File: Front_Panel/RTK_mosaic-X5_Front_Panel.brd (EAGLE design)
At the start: 158.6 x 41 mm, 29 parts

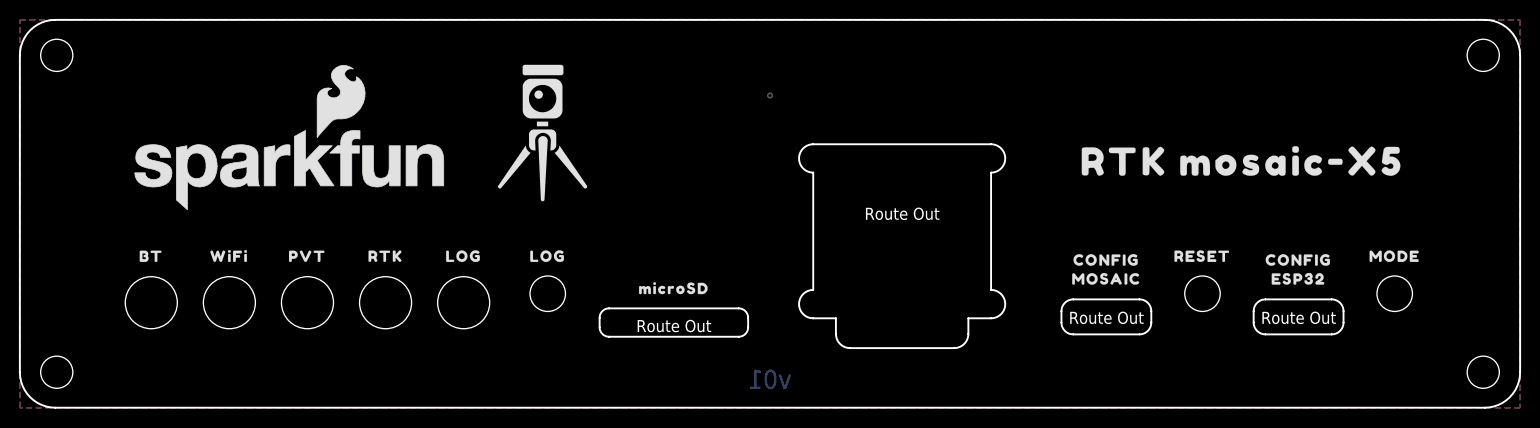
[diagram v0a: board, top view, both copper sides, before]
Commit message: Update front panel with new 1.3" OLED
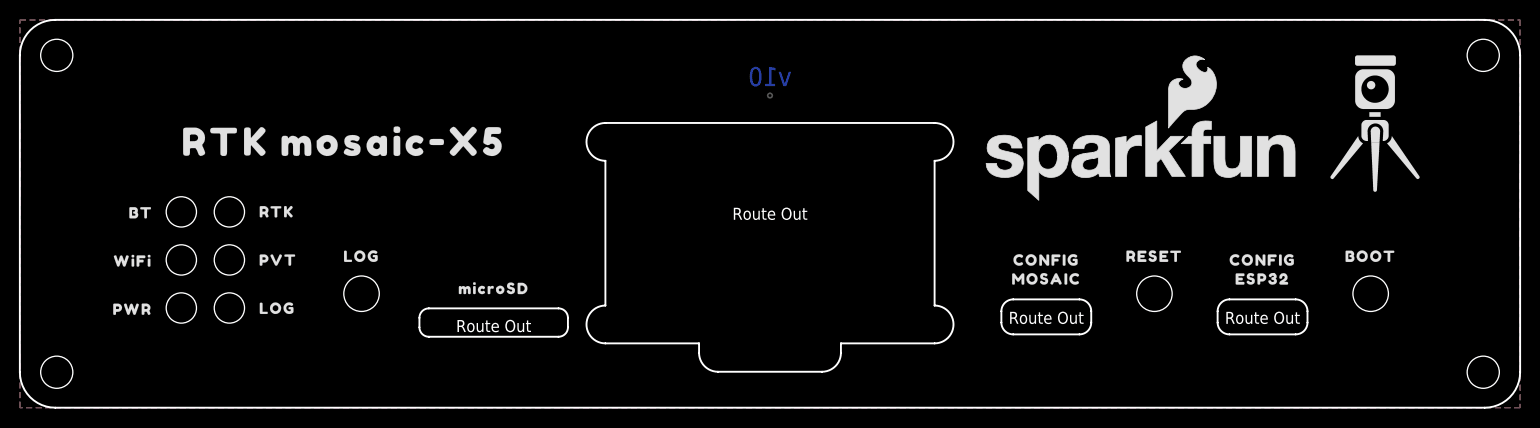
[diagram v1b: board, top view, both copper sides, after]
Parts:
- removed LED, LED5, LED6, LED7, LED8: LED_DIO-13847, SparkFun-Enclosure-Panel:LED
- removed U$2: (no value), output:MODE0
- added U$16, U$5: CBI_LED_TRIPLE-3MM_DIO-19990, SparkFun-Enclosure-Panel:CBI_LED_TRIPLE-3MM
- added U$17: (no value), output:PWR0
- added U$18: (no value), output:BOOT0
- OLED: value OLED_14532 -> OLED_1.3_128X64; device SparkFun-Enclosure-Panel:OLED -> SparkFun-Enclosure-Panel:OLED-1.3-128X64
- moved U$15 95.0 mm to (-45.0, 20.1)
- moved LOGO1 90.0 mm to (39.1, 18.1)
- moved U$6 20.5 mm to (-52.1, 2.50)
- moved RESET1 19.7 mm to (-43.2, 0.00)
- moved U$4 19.7 mm to (-43.2, 8.00)
- moved MICRO_SD 19.1 mm to (-29.2, 0.00)
- moved U$7 19.1 mm to (-29.2, 4.60)
- moved OLED 14.0 mm to (0.00, 12.5)
- moved U$14 12.4 mm to (-52.1, 12.7)
- moved U$12 10.2 mm to (-67.3, 7.50)
- moved ESP32_USB 6.35 mm to (29.2, 0.00)
- moved U$1 6.35 mm to (29.2, 5.60)
- moved U$9 6.35 mm to (29.2, 7.60)
- moved RESET 5.08 mm to (40.6, 0.00)
- moved U$8 5.08 mm to (40.6, 8.00)
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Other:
- board text added: "v10"
- board text removed: "v01"
